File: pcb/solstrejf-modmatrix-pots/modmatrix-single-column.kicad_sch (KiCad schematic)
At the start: 12 parts

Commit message: updated pcb layout
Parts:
- RV1: value R_Potentiometer -> B10k
- RV10, RV11, RV12, RV2, RV3, RV4, RV5, RV6, RV7, RV8, RV9: value R_Potentiometer -> B10K
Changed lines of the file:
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@@
 			)
 		)
-		(property "Value" "R_Potentiometer"
+		(property "Value" "B10K"
 			(at 213.36 83.8199 0)
 			(effects
@@
 			)
 		)
-		(property "Value" "R_Potentiometer"
+		(property "Value" "B10K"
 			(at 86.36 134.6199 0)
 			(effects
@@
 			)
 		)
-		(property "Value" "R_Potentiometer"
+		(property "Value" "B10K"
 			(at 149.86 134.6199 0)
 			(effects
@@
 			)
 		)
-		(property "Value" "R_Potentiometer"
+		(property "Value" "B10K"
 			(at 149.86 109.2199 0)
 			(effects
@@
 			)
 		)
-		(property "Value" "R_Potentiometer"
+		(property "Value" "B10K"
 			(at 213.36 58.4199 0)
 			(effects
@@
 			)
 		)
-		(property "Value" "R_Potentiometer"
+		(property "Value" "B10K"
 			(at 213.36 109.2199 0)
 			(effects
@@
 			)
 		)
-		(property "Value" "R_Potentiometer"
+		(property "Value" "B10K"
 			(at 86.36 83.8199 0)
 			(effects
@@
 			)
 		)
-		(property "Value" "R_Potentiometer"
+		(property "Value" "B10K"
 			(at 149.86 58.4199 0)
 			(effects
@@
 			)
 		)
-		(property "Value" "R_Potentiometer"
+		(property "Value" "B10K"
 			(at 86.36 109.2199 0)
 			(effects
@@
 			)
 		)
-		(property "Value" "R_Potentiometer"
+		(property "Value" "B10K"
 			(at 149.86 83.8199 0)
 			(effects
@@
 			)
 		)
-		(property "Value" "R_Potentiometer"
+		(property "Value" "B10k"
 			(at 86.36 58.4199 0)
 			(effects
@@
 			)
 		)
-		(property "Value" "R_Potentiometer"
+		(property "Value" "B10K"
 			(at 213.36 134.6199 0)
 			(effects

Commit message: Added kromftronics custom kicad files as submodule. Updated modmatrix KiCad project to use the submodule.
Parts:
- RV1, RV10, RV11, RV12, RV2, RV3, RV4, RV5, RV6, RV7, RV8, RV9: footprint Kromtronics_Custom:Potentiometer_Alpha_slide_pot_30mm -> Kromftronics_Custom:Potentiometer_Alpha_slide_pot_30mm

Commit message: Updated sheet titles in modulation matrix and exported current rev1.0 schematic
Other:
- title: (none) -> Modulation Matrix - One Voice
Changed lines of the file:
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@@
 	(generator_version "8.0")
 	(paper "A4")
+	(title_block
+		(title "Modulation Matrix - One Voice")
+		(date "2024-08-24")
+		(rev "1.0")
+	)
 	(wire
 		(pts
@@
 		(dnp no)
 		(fields_autoplaced yes)
-		(property "Reference" "#PWR013"
+		(property "Reference" "#PWR01"
 			(at 88.9 69.85 0)
 			(effects

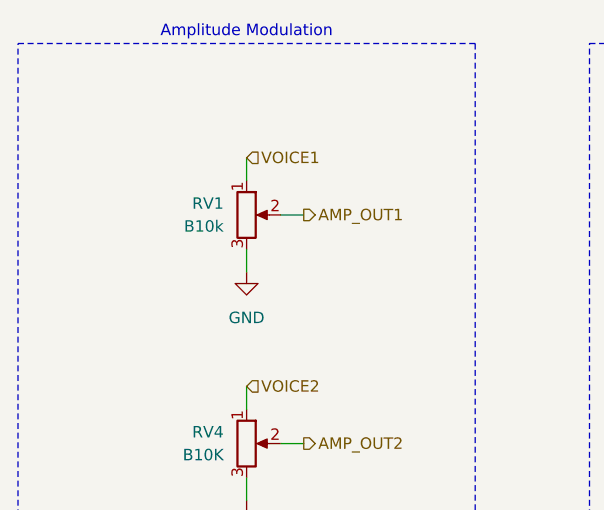
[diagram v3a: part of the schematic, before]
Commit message: Updated potentiometer value from B10k to B10K in order for all of the slide pots to have the same value in the BOM. Generated ibom for the mod-matrix board.
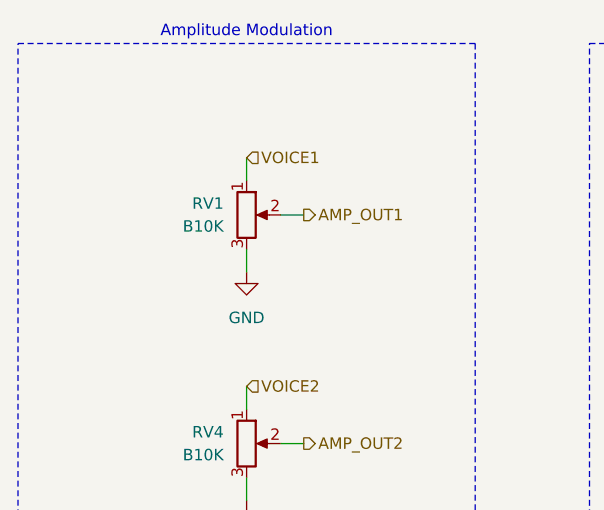
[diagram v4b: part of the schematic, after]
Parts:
- RV1: value B10k -> B10K
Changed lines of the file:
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@@
 			)
 		)
-		(property "Value" "B10k"
+		(property "Value" "B10K"
 			(at 86.36 58.4199 0)
 			(effects
